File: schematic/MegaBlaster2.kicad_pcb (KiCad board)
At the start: 4 copper layers, 99 x 99 mm, 120 parts, among them J1 USB_B, J2 SWD, J3 Micro_SD_Card, J4 AudioJack3, SW2 SW_Push_Dual, SW3 SW_Push_Dual, SW4 SW_Push_Dual, SW5 SW_Push_Dual, SW6 SW_Push_Dual, SW7 SW_Push_Dual, SW8 YM_SELECTION, U1 ATSAMD51J19A-A, U10 TPA6111A2DR, U11 NE5532, U2 LM2733XMF, U3 LD1117S33TR_SOT223, U4 LD1117S50TR_SOT223, U5 W25Q32JVSS, U6 Si5351A-B-GT, U7 RAM_EXP, U8 YM2612, U9 SN76489, Y1 32.768KHz, Y2 25MHz

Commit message: schematic v1
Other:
- net class Default removed
- net class THICC removed

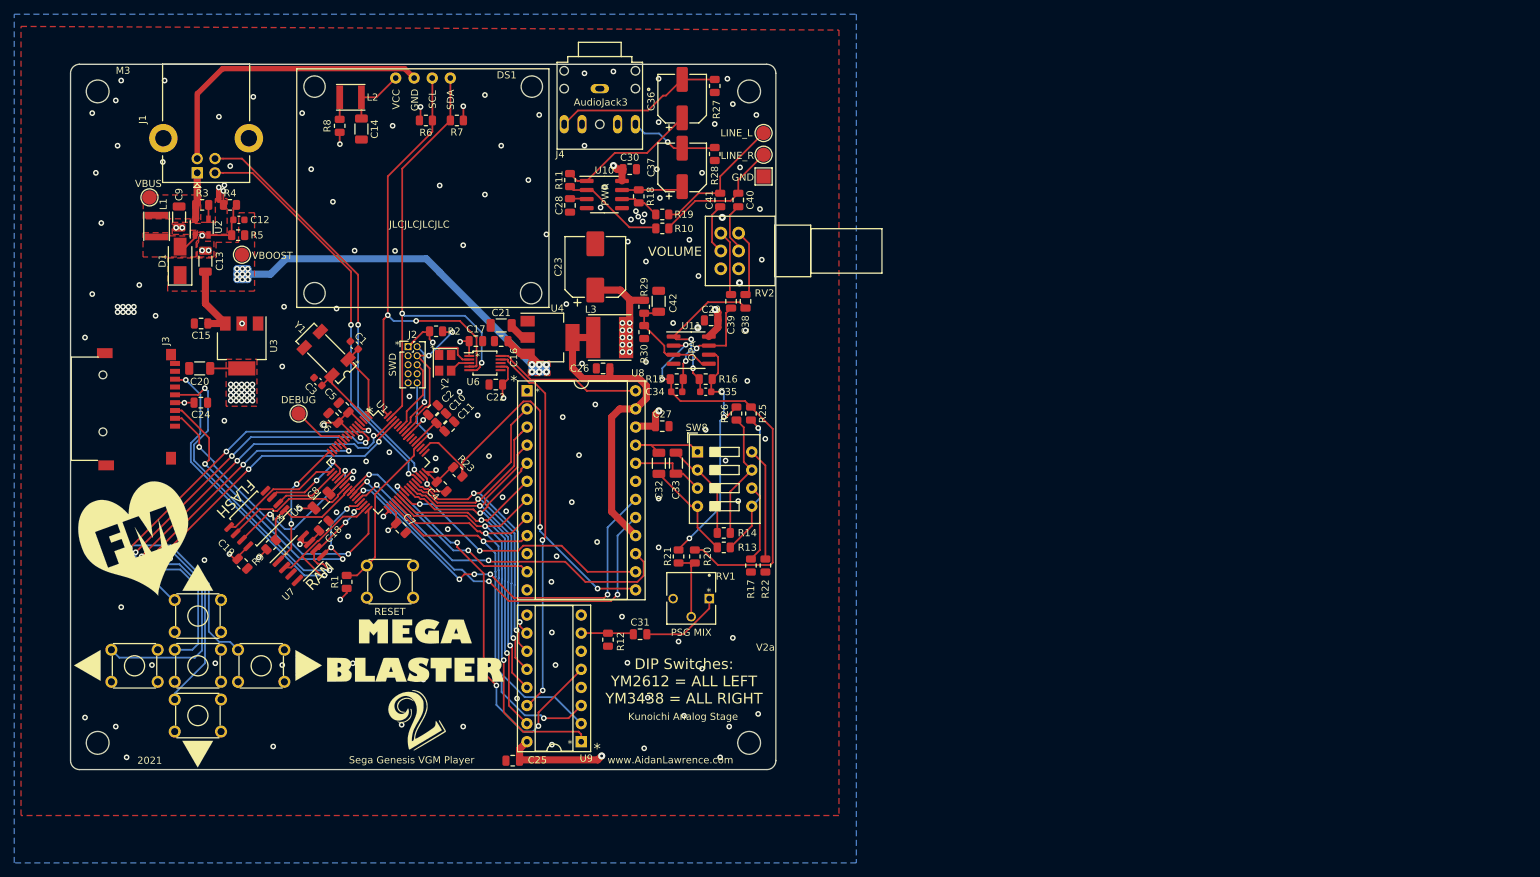
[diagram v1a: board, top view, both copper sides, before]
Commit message: remove old traces and devices
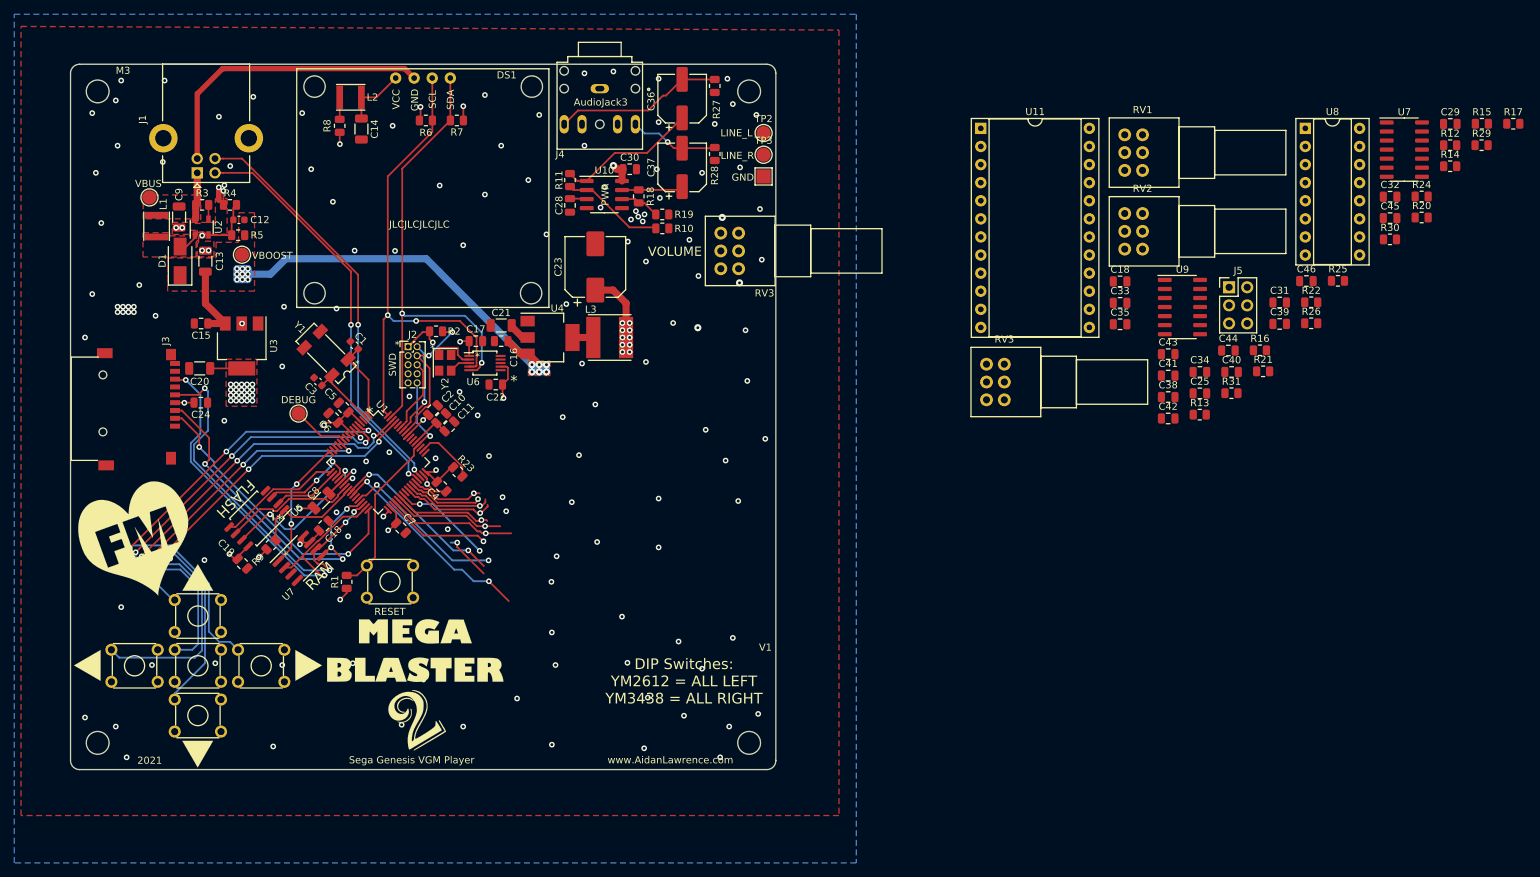
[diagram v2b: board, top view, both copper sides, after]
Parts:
- removed C26, C27: 100nF, Capacitor_SMD:C_0805_2012Metric
- removed SW8: YM_SELECTION, Button_Switch_THT:SW_DIP_SPSTx04_Slide_9.78x12.34mm_W7.62mm_P2.54mm
- added C18: 100nF, Capacitor_SMD:C_0805_2012Metric, F.Cu at (231.1, 72.4)
- added C43: 1uF, Capacitor_SMD:C_0805_2012Metric, F.Cu at (237.9, 82.6)
- added C44: 1uF, Capacitor_SMD:C_0805_2012Metric, F.Cu at (246.3, 82.1)
- added C45: 1uF, Capacitor_SMD:C_0805_2012Metric, F.Cu at (269.0, 63.5)
- added C46: 1uF, Capacitor_SMD:C_0805_2012Metric, F.Cu at (257.3, 72.3)
- added J5: DAC_Enable, Connector_PinHeader_2.54mm:PinHeader_2x03_P2.54mm_Vertical, F.Cu at (246.4, 73.2)
- added R24: 1M, Resistor_SMD:R_0805_2012Metric, F.Cu at (273.5, 60.5)
- added R31: 10K, Resistor_SMD:R_0805_2012Metric, F.Cu at (246.8, 88.1)
- added RV2: 10K, Potentiometer_THT:Potentiometer_Alps_RK097_Dual_Horizontal, F.Cu at (234.3, 67.9)
- added RV3: 10K, Potentiometer_THT:Potentiometer_Alps_RK097_Dual_Horizontal, F.Cu at (214.9, 89.0)
- added U7: TL074, Package_SO:SOIC-14_3.9x8.7mm_P1.27mm, F.Cu at (271.0, 53.9)
- C25: value 100nF -> 1uF
- C29: value 100nF -> 3.3nF
- C32, C33: value 10uF -> 100nF; footprint Capacitor_SMD:C_1206_3216Metric -> Capacitor_SMD:C_0805_2012Metric
- C34: value 120pF -> 1uF; footprint Capacitor_SMD:C_0603_1608Metric -> Capacitor_SMD:C_0805_2012Metric
- C35: value 120pF -> 3.3nF; footprint Capacitor_SMD:C_0603_1608Metric -> Capacitor_SMD:C_0805_2012Metric
- C42: value 10uF -> 1uF; footprint Capacitor_SMD:C_1206_3216Metric -> Capacitor_SMD:C_0805_2012Metric
- R12: value 2K2 -> 100R
- R13: value 47K -> 1M
- R14: value 47K -> 10K
- R15: value 82K -> 1M
- R16: value 82K -> 10K
- R17: value 2K2 -> 1M
- R20, R21: value 100K -> 10K
- R22: value 2K2 -> 10K
- R25, R26: value 5K6 -> 10K
- RV1: value 100K -> 10K; footprint bourns:3362P-1-103LF -> Potentiometer_THT:Potentiometer_Alps_RK097_Dual_Horizontal
- U11: value NE5532 -> YM2151; footprint Package_SO:SOIC-8_3.9x4.9mm_P1.27mm -> Package_DIP:DIP-24_W15.24mm_Socket
- U8: value YM2612 -> YM3012; footprint Package_DIP:DIP-24_W15.24mm_Socket -> Package_DIP:DIP-16_W7.62mm_Socket
- U9: value SN76489 -> MCP6004; footprint Package_DIP:DIP-16_W7.62mm_Socket -> Package_SO:SOIC-14_3.9x8.7mm_P1.27mm
- moved R12 137.1 mm to (277.5, 53.3), turned to 0 degrees
- moved R17 123.7 mm to (286.3, 50.3), turned to 0 degrees
- moved R29 119.7 mm to (281.9, 53.3), turned to 0 degrees
- moved R15 118.6 mm to (281.9, 50.3)
- moved U8 115.3 mm to (257.1, 50.9)
- moved R14 114.2 mm to (277.5, 56.2), turned to 0 degrees
- moved R20 112.6 mm to (273.5, 63.4), turned to 0 degrees
- moved C25 109.4 mm to (242.3, 88.1), turned to 0 degrees
- moved C32 109.3 mm to (269.0, 60.5), turned to 0 degrees
- moved C29 107.4 mm to (277.5, 50.3), turned to 0 degrees
- moved R30 105.5 mm to (269.0, 66.5), turned to 0 degrees
- moved U9 104.1 mm to (239.9, 76.0), turned to 0 degrees
- moved C31 101.1 mm to (253.5, 75.3)
- moved RV1 89.1 mm to (234.3, 56.8), turned to 0 degrees
- moved R21 86.1 mm to (251.2, 85.0), turned to 0 degrees
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- renumbered RV2 to RV3
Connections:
- C25 pad 1: +5VA -> Net-(C25-Pad1)
- C25 pad 2: GND -> Net-(C25-Pad2)
- C29 pad 1: +5VA -> Net-(C29-Pad1)
- C31 pad 1: PSG_OUT -> Net-(C31-Pad1)
- C32 pad 1: MOL -> GND
- C32 pad 2: BPL -> +5VA
- C33 pad 1: MOR -> +5VA
- C33 pad 2: BPR -> GND
- C34 pad 2: SELECT_L -> Net-(C34-Pad2)
- C35 pad 2: SELECT_R -> GND
- C38 pad 2: Net-(C34-Pad1) -> Net-(C38-Pad2)
- C39 pad 2: Net-(C35-Pad1) -> Net-(C39-Pad2)
- C40 pad 1: LINE_L -> Net-(C40-Pad1)
- C41 pad 1: LINE_R -> Net-(C41-Pad1)
- C42 pad 1: +2V5 -> MIX_L
- C42 pad 2: GND -> Net-(C42-Pad2)
- J2 pad 7: Net-(J2-Pad7) -> unconnected-(J2-Pad7)
- J2 pad 8: Net-(J2-Pad8) -> unconnected-(J2-Pad8)
- J2 pad 9: Net-(J2-Pad9) -> unconnected-(J2-Pad9)
- J3 pad 1: Net-(J3-Pad1) -> unconnected-(J3-Pad1)
- J3 pad 8: Net-(J3-Pad8) -> unconnected-(J3-Pad8)
- R10 pad 1: LINE_L -> MIX_L
- R12 pad 1: GND -> Net-(R12-Pad1)
- R12 pad 2: PSG_OUT -> Net-(R12-Pad2)
- R13 pad 1: Net-(R13-Pad1) -> +2V5
- R13 pad 2: BPL -> Net-(C31-Pad1)
- R14 pad 1: Net-(R14-Pad1) -> Net-(C31-Pad1)
- R14 pad 2: BPR -> DAC_R
- R15 pad 1: SELECT_L -> +2V5
- R15 pad 2: Net-(C34-Pad1) -> Net-(C38-Pad1)
- R16 pad 1: SELECT_R -> Net-(C38-Pad1)
- R16 pad 2: Net-(C35-Pad1) -> DAC_L
- R17 pad 1: GND -> +2V5
- R17 pad 2: Net-(R17-Pad2) -> Net-(C40-Pad1)
- R19 pad 2: LINE_R -> MIX_R
- R20 pad 1: SELECT_L -> Net-(R20-Pad1)
- R20 pad 2: Net-(R20-Pad2) -> DAC_L
- R21 pad 1: Net-(R20-Pad2) -> Net-(C41-Pad2)
- R21 pad 2: SELECT_R -> Net-(R21-Pad2)
- R22 pad 2: Net-(R22-Pad2) -> Net-(R21-Pad2)
- R25 pad 1: SELECT_L -> Net-(R25-Pad1)
- R25 pad 2: Net-(R13-Pad1) -> DAC_R
- R26 pad 1: Net-(R14-Pad1) -> Net-(C45-Pad2)
- R26 pad 2: SELECT_R -> Net-(R26-Pad2)
- R29 pad 1: +5VA -> GND
- R29 pad 2: +2V5 -> Net-(R26-Pad2)
- R30 pad 1: +2V5 -> Net-(J5-Pad5)
- RV1 pad 1: Net-(C31-Pad2) -> GND
- RV1 pad 2: Net-(R20-Pad2) -> Net-(C31-Pad2)
- RV1 pad 3: Net-(RV1-Pad3) -> Net-(C25-Pad1)
- SW2 pad 2: Net-(SW2-Pad2) -> unconnected-(SW2-Pad2)
- SW2 pad 3: Net-(SW2-Pad3) -> unconnected-(SW2-Pad3)
- SW3 pad 2: Net-(SW3-Pad2) -> unconnected-(SW3-Pad2)
- SW3 pad 3: Net-(SW3-Pad3) -> unconnected-(SW3-Pad3)
- SW4 pad 2: Net-(SW4-Pad2) -> unconnected-(SW4-Pad2)
- SW4 pad 3: Net-(SW4-Pad3) -> unconnected-(SW4-Pad3)
- SW5 pad 2: Net-(SW5-Pad2) -> unconnected-(SW5-Pad2)
- SW5 pad 3: Net-(SW5-Pad3) -> unconnected-(SW5-Pad3)
- SW6 pad 2: Net-(SW6-Pad2) -> unconnected-(SW6-Pad2)
- SW6 pad 3: Net-(SW6-Pad3) -> unconnected-(SW6-Pad3)
- SW7 pad 2: Net-(SW7-Pad2) -> unconnected-(SW7-Pad2)
- SW7 pad 3: Net-(SW7-Pad3) -> unconnected-(SW7-Pad3)
- TP2 pad 1: LINE_L -> MIX_L
- TP3 pad 1: LINE_R -> MIX_R
- U1 pad 13: Net-(U1-Pad13) -> unconnected-(U1-Pad13)
- U1 pad 15: Net-(U1-Pad15) -> unconnected-(U1-Pad15)
- U1 pad 16: RAM_CS -> unconnected-(U1-Pad16)
- U1 pad 27: YM_A1 -> unconnected-(U1-Pad27)
- U1 pad 40: PSG_WE -> unconnected-(U1-Pad40)
- U1 pad 55: Net-(U1-Pad55) -> unconnected-(U1-Pad55)
- U1 pad 60: Net-(U1-Pad60) -> unconnected-(U1-Pad60)
- U11 pad 1: Net-(C34-Pad1) -> GND
- U11 pad 2: SELECT_L -> YM_IRQ
- U11 pad 3: +2V5 -> YM_IC
- U11 pad 4: GND -> YM_A0
- U11 pad 5: +2V5 -> YM_WR
- U11 pad 6: SELECT_R -> +5V
- U11 pad 7: Net-(C35-Pad1) -> YM_CS
- U11 pad 8: +5VA -> unconnected-(U11-Pad8)
- U6 pad 6: Net-(U6-Pad6) -> unconnected-(U6-Pad6)
- U6 pad 9: PSG_CLK -> unconnected-(U6-Pad9)
- U8 pad 1: GND -> +5VA
- U8 pad 10: Net-(U8-Pad10) -> Net-(C29-Pad1)
- U8 pad 11: YM_IC -> Net-(R12-Pad2)
- U8 pad 12: GND -> Net-(U7-Pad5)
- U8 pad 13: YM_IRQ -> +2V5
- U8 pad 14: YM_CS -> Net-(U7-Pad2)
- U8 pad 15: YM_WR -> Net-(U7-Pad3)
- U8 pad 16: +5V -> GND
- U8 pad 2: D0 -> DAC_CLK
- U8 pad 3: D1 -> GND
- U8 pad 4: D2 -> SO
- U8 pad 5: D3 -> SH2
- U8 pad 6: D4 -> SH1
- U8 pad 7: D5 -> YM_IC
- U8 pad 8: D6 -> GND
- U8 pad 9: D7 -> Net-(C35-Pad1)
- U9 pad 1: D5 -> Net-(R20-Pad1)
- U9 pad 10: D0 -> DAC_L
- U9 pad 11: D1 -> GND
- U9 pad 12: D2 -> DAC_R
- U9 pad 13: D3 -> Net-(R26-Pad2)
- U9 pad 14: PSG_CLK -> Net-(C45-Pad2)
- U9 pad 2: D6 -> Net-(R20-Pad1)
- U9 pad 3: D7 -> Net-(C40-Pad1)
- U9 pad 4: Net-(U9-Pad4) -> +5VA
- U9 pad 5: PSG_WE -> Net-(C44-Pad1)
- U9 pad 6: GND -> Net-(R25-Pad1)
- U9 pad 7: PSG_OUT -> Net-(R25-Pad1)
- U9 pad 8: GND -> Net-(C41-Pad2)
- U9 pad 9: Net-(U9-Pad9) -> Net-(R21-Pad2)
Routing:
- net SELECT_L: track 58.0 -> 0.00 mm, vias 2 -> 0
- net YM_A1: track 57.7 -> 0.00 mm, vias 5 -> 0
- net PSG_WE: track 56.7 -> 0.00 mm, vias 4 -> 0
- net PSG_CLK: track 53.3 -> 0.00 mm, vias 2 -> 0
- net YM_IRQ: track 59.4 -> 8.69 mm, vias 2 -> 0
- net D5: track 61.8 -> 16.1 mm, vias 2 -> 1
- net +5V: track 48.8 -> 5.78 mm
- net D7: track 57.0 -> 16.1 mm, vias 2 -> 1
- net D4: track 53.2 -> 13.7 mm, vias 2 -> 1
- net D6: track 56.0 -> 18.1 mm
- net D0: track 48.1 -> 10.4 mm, vias 2 -> 1
- net D1: track 48.0 -> 10.5 mm, vias 2 -> 1
- net D3: track 49.1 -> 13.4 mm, vias 2 -> 1
- net D2: track 48.1 -> 12.5 mm, vias 2 -> 1
- net SELECT_R: track 35.5 -> 0.00 mm, vias 3 -> 0
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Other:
- board text added: "2022 Aidan Lawrence www.aidanlawrence.com"
- board text added: "V1"
- board text removed: "2021 Aidan Lawrence www.aidanlawrence.com Analog stage schematic courtesy of: KUNOICHI LABS kunoichilabs.dev"
- board text removed: "Kunoichi Analog Stage"
- board text removed: "OPA"
- board text removed: "PSG MIX"
- board text removed: "V2a"

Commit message: PCB first pass
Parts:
- removed the C18 at (119.4, 106.7)
- removed the G*** at (132.1, 127.5)
- removed the RV3 at (177.6, 70.6)
- removed the RV3 at (214.9, 89.0)
- removed the U7 at (116.1, 111.3)
- added C26: 100nF, Capacitor_SMD:C_0805_2012Metric, F.Cu at (155.7, 85.0)
- added C27: 100nF, Capacitor_SMD:C_0805_2012Metric, F.Cu at (159.1, 119.9)
- added G***: LOGO, Art:ArcadeClassicLogo, F.Cu at (131.8, 128.0)
- added G***: LOGO, Art:PCM_Logo_Mask, F.Cu at (88.6, 64.0)
- added RV3: 10K, Potentiometer_THT:Potentiometer_Alps_RK097_Dual_Horizontal, F.Cu at (177.6, 67.8)
- moved R12 144.3 mm to (158.1, 134.4), turned to -90 degrees
- moved R30 137.5 mm to (142.6, 120.7), turned to -90 degrees
- moved C29 135.8 mm to (169.2, 132.3)
- moved U7 132.3 mm to (163.4, 130.8)
- moved U8 129.4 mm to (147.3, 119.4)
- moved J5 118.4 mm to (135.9, 115.6), turned to 90 degrees
- moved R15 116.4 mm to (174.5, 95.0), turned to -90 degrees
- moved R17 114.8 mm to (180.6, 95.0), turned to -90 degrees
- moved R29 107.8 mm to (176.4, 75.6), turned to -90 degrees
- moved R31 107.3 mm to (144.5, 120.7), turned to -90 degrees
- moved R14 106.1 mm to (176.5, 88.8), turned to 90 degrees
- moved C32 105.9 mm to (164.3, 76.7), turned to -90 degrees
- moved C39 101.9 mm to (170.8, 137.8), turned to 180 degrees
- moved R24 101.0 mm to (178.6, 95.0), turned to -90 degrees
- moved R20 98.3 mm to (176.4, 79.0), turned to 90 degrees
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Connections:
- U1 pad 35: D7 -> D0
- U1 pad 36: D6 -> D1
- U1 pad 37: D5 -> D2
- U1 pad 38: D4 -> D3
- U1 pad 41: D3 -> D4
- U1 pad 42: D2 -> D5
- U1 pad 43: D1 -> D6
- U1 pad 44: D0 -> D7
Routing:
- net +2V5: track 0.00 -> 58.0 mm, vias 0 -> 1
- net Net-(C39-Pad2): track 0.00 -> 57.3 mm
- net Net-(C43-Pad2): track 0.00 -> 54.0 mm
- net Net-(C40-Pad1): track 0.00 -> 47.5 mm, vias 0 -> 2
- net YM_IC: track 25.1 -> 72.4 mm, vias 2 -> 1
- net Net-(C44-Pad1): track 0.00 -> 45.5 mm, vias 0 -> 2
- net DAC_CLK: track 0.00 -> 42.5 mm, vias 0 -> 1
- net SH1: track 0.00 -> 41.3 mm, vias 0 -> 2
- net +5V: track 5.78 -> 46.6 mm
- net +5VA: track 13.2 -> 52.2 mm, vias 11 -> 13
- net SO: track 0.00 -> 38.7 mm, vias 0 -> 1
- net SH2: track 0.00 -> 38.3 mm, vias 0 -> 1
- net DAC0: track 0.00 -> 35.2 mm, vias 0 -> 1
- net DAC1: track 0.00 -> 29.1 mm, vias 0 -> 1
- net D2: track 12.5 -> 38.0 mm, vias 1 -> 0
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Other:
- board text added: "2022"
- board text added: "DAC ENABLE"
- board text added: "DAC MIX"
- board text added: "FM MIX"
- board text added: "OFF"
- board text added: "ON"
- board text added: "YM2151 VGM Player"
- board text removed: "...oh and 3 channels of square waves and 1 channel of noise. TY PSG"
- board text removed: "2021"
- board text removed: "DIP Switches: YM2612 = ALL LEFT YM3438 = ALL RIGHT"
- board text removed: "RAM"
- board text removed: "Sega Genesis VGM Player"

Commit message: PCB v1
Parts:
- removed the G*** at (133.3, 70.4)
- removed the G*** at (133.3, 99.0)
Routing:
- net GND: vias 162 -> 164
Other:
- board text added: "YM2151 + PCM VGM Player"
- board text removed: "YM2151 VGM Player"

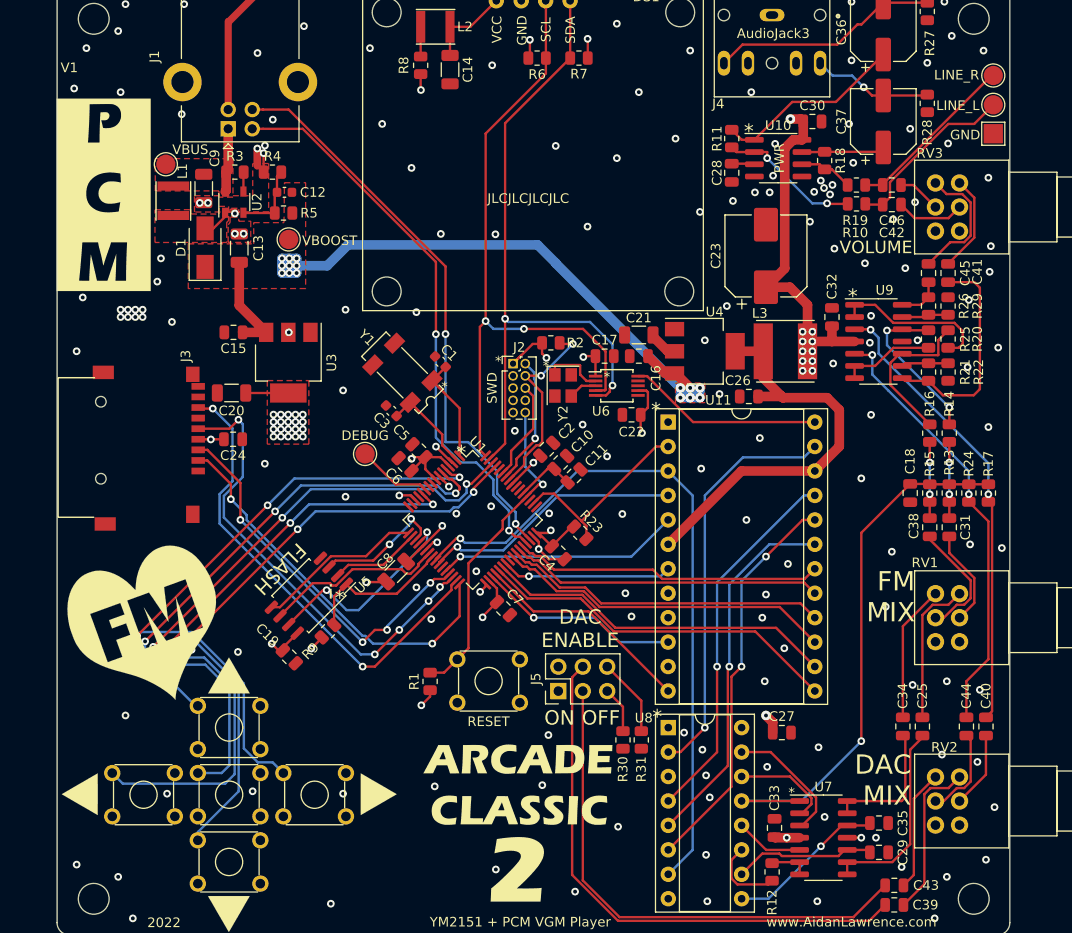
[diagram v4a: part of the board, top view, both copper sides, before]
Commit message: 2M resistor update
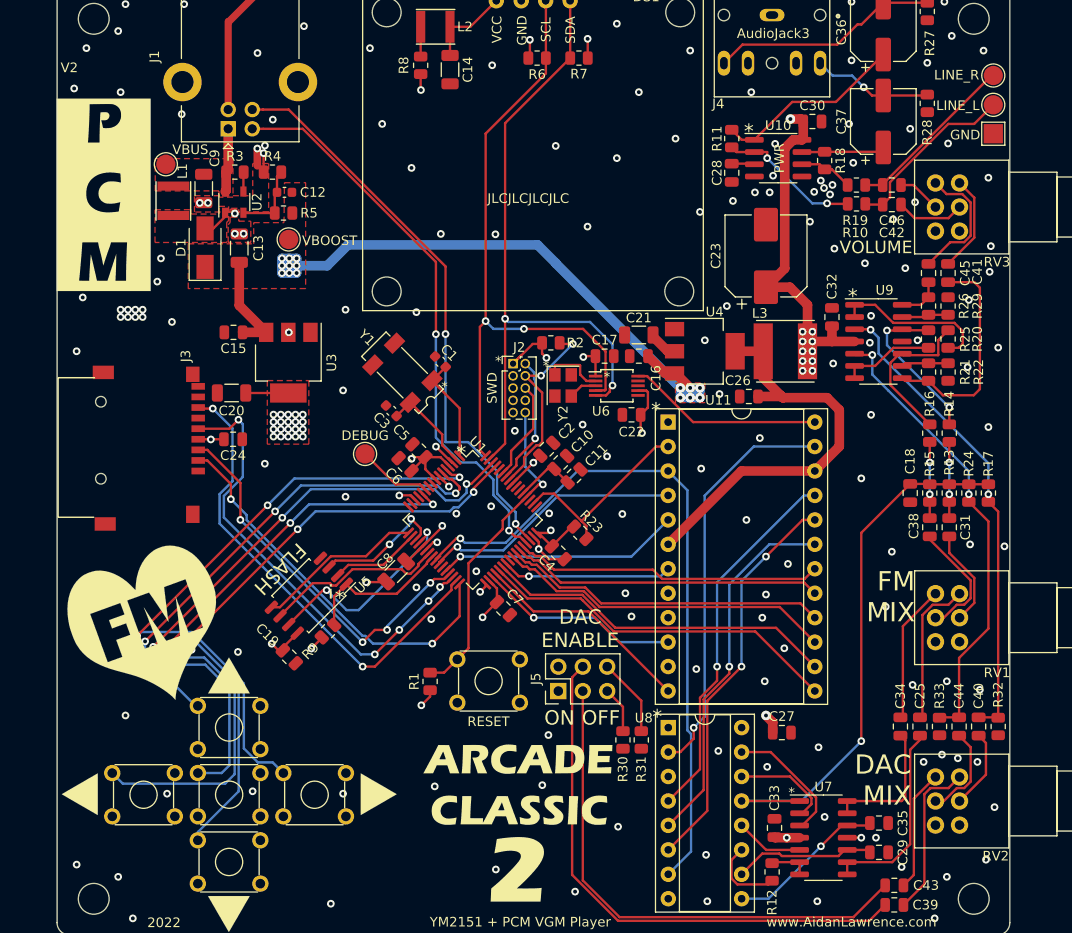
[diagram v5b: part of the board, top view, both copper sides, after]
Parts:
- added R32: 2M, Resistor_SMD:R_0805_2012Metric, F.Cu at (181.6, 119.3)
- added R33: 2M, Resistor_SMD:R_0805_2012Metric, F.Cu at (175.5, 119.3)
- U7: value TL074 -> MCP6004
- moved C40 0.76 mm to (179.6, 119.3)
- moved C44 0.76 mm to (177.5, 119.3)
- moved C34 0.25 mm to (171.4, 119.3)
- moved C25 0.25 mm to (173.5, 119.3)
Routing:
- net Net-(R24-Pad2): track 45.5 -> 47.9 mm
- net Net-(C40-Pad1): track 47.5 -> 49.5 mm
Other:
- board text added: "V2"
- board text removed: "V1"
